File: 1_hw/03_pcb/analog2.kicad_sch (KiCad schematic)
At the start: 19 parts, among them U22 TPL0401B-10, U23 THS3491, U24 ADG1219BRJZ

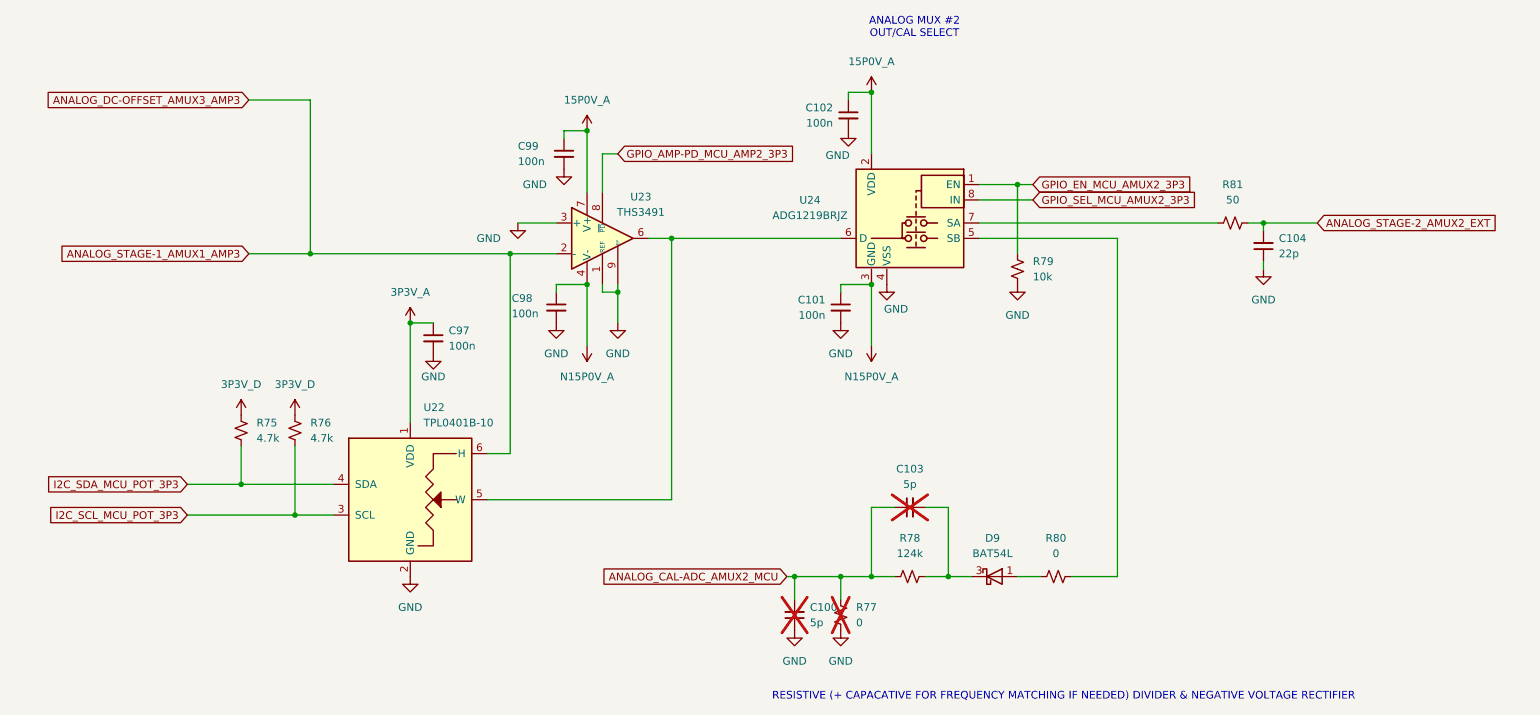
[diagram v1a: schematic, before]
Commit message: FEAT: Initial board placement started.
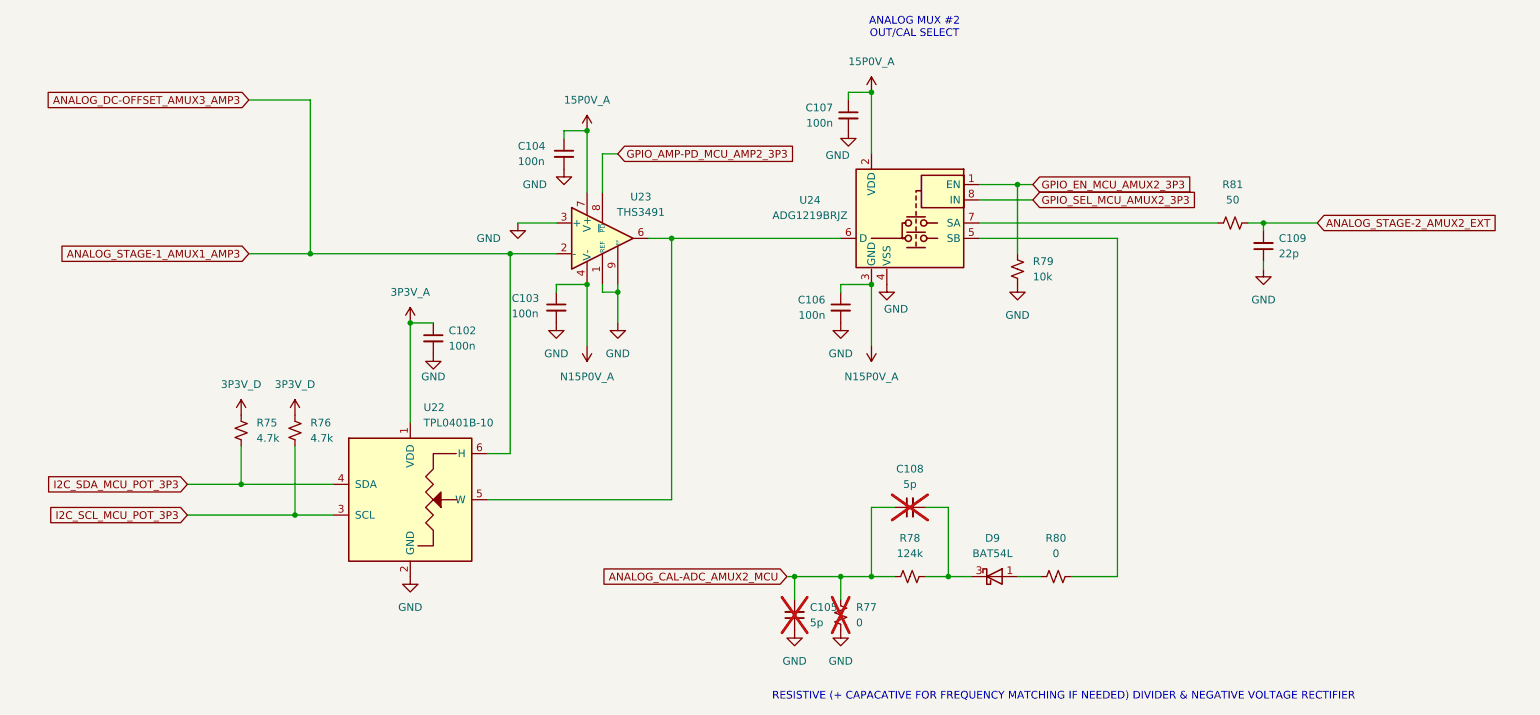
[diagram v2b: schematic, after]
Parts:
- renumbered C97 to C102, C98 to C103, C99 to C104, C100 to C105, C101 to C106, C102 to C107, C103 to C108, C104 to C109
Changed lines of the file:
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@@
 		(dnp no)
 		(fields_autoplaced yes)
-		(property "Reference" "#PWR0260"
+		(property "Reference" "#PWR0272"
 			(at 152.4 104.14 0)
 			(effects
@@
 			(project "arb"
 				(path "/866ef9be-3b01-4288-a6e0-a2357aa17e50/e46c6640-71a3-4b78-b602-0f6be9676e36"
-					(reference "#PWR0260")
+					(reference "#PWR0272")
 					(unit 1)
 				)
@@
 		(dnp no)
 		(fields_autoplaced yes)
-		(property "Reference" "#PWR0261"
+		(property "Reference" "#PWR0273"
 			(at 152.4 154.94 0)
 			(effects
@@
 			(project "arb"
 				(path "/866ef9be-3b01-4288-a6e0-a2357aa17e50/e46c6640-71a3-4b78-b602-0f6be9676e36"
-					(reference "#PWR0261")
+					(reference "#PWR0273")
 					(unit 1)
 				)
@@
 		(dnp no)
 		(fields_autoplaced yes)
-		(property "Reference" "#PWR0257"
+		(property "Reference" "#PWR0269"
 			(at 110.49 97.79 0)
 			(effects
@@
 			(project "arb"
 				(path "/866ef9be-3b01-4288-a6e0-a2357aa17e50/e46c6640-71a3-4b78-b602-0f6be9676e36"
-					(reference "#PWR0257")
+					(reference "#PWR0269")
 					(unit 1)
 				)
@@
 		(dnp no)
 		(fields_autoplaced yes)
-		(property "Reference" "C102"
+		(property "Reference" "C107"
 			(at 151.13 62.2363 0)
 			(effects
@@
 			(project "arb"
 				(path "/866ef9be-3b01-4288-a6e0-a2357aa17e50/e46c6640-71a3-4b78-b602-0f6be9676e36"
-					(reference "C102")
+					(reference "C107")
 					(unit 1)
 				)
@@
 		(dnp no)
 		(fields_autoplaced yes)
-		(property "Reference" "#PWR0259"
+		(property "Reference" "#PWR0271"
 			(at 144.78 154.94 0)
 			(effects
@@
 			(project "arb"
 				(path "/866ef9be-3b01-4288-a6e0-a2357aa17e50/e46c6640-71a3-4b78-b602-0f6be9676e36"
-					(reference "#PWR0259")
+					(reference "#PWR0271")
 					(unit 1)
 				)
@@
 		(on_board yes)
 		(dnp no)
-		(property "Reference" "#PWR0262"
+		(property "Reference" "#PWR0274"
 			(at 153.67 72.39 0)
 			(effects
@@
 			(project "arb"
 				(path "/866ef9be-3b01-4288-a6e0-a2357aa17e50/e46c6640-71a3-4b78-b602-0f6be9676e36"
-					(reference "#PWR0262")
+					(reference "#PWR0274")
 					(unit 1)
 				)
@@
 		(dnp yes)
 		(fields_autoplaced yes)
-		(property "Reference" "C100"
+		(property "Reference" "C105"
 			(at 147.32 144.7735 0)
 			(effects
@@
 			(project "arb"
 				(path "/866ef9be-3b01-4288-a6e0-a2357aa17e50/e46c6640-71a3-4b78-b602-0f6be9676e36"
-					(reference "C100")
+					(reference "C105")
 					(unit 1)
 				)
@@
 		(on_board yes)
 		(dnp no)
-		(property "Reference" "C99"
+		(property "Reference" "C104"
 			(at 99.06 68.58 0)
 			(effects
@@
 			(project "arb"
 				(path "/866ef9be-3b01-4288-a6e0-a2357aa17e50/e46c6640-71a3-4b78-b602-0f6be9676e36"
-					(reference "C99")
+					(reference "C104")
 					(unit 1)
 				)
@@
 		(dnp no)
 		(fields_autoplaced yes)
-		(property "Reference" "C101"
+		(property "Reference" "C106"
 			(at 149.86 93.9863 0)
 			(effects
@@
 			(project "arb"
 				(path "/866ef9be-3b01-4288-a6e0-a2357aa17e50/e46c6640-71a3-4b78-b602-0f6be9676e36"
-					(reference "C101")
+					(reference "C106")
 					(unit 1)
 				)
@@
 		(dnp no)
 		(fields_autoplaced yes)
-		(property "Reference" "#PWR0258"
+		(property "Reference" "#PWR0270"
 			(at 115.57 104.14 0)
 			(effects
@@
 			(project "arb"
 				(path "/866ef9be-3b01-4288-a6e0-a2357aa17e50/e46c6640-71a3-4b78-b602-0f6be9676e36"
-					(reference "#PWR0258")
+					(reference "#PWR0270")
 					(unit 1)
 				)
@@
 		(on_board yes)
 		(dnp no)
-		(property "Reference" "#PWR0255"
+		(property "Reference" "#PWR0267"
 			(at 106.68 78.74 0)
 			(effects
@@
 			(project "arb"
 				(path "/866ef9be-3b01-4288-a6e0-a2357aa17e50/e46c6640-71a3-4b78-b602-0f6be9676e36"
-					(reference "#PWR0255")
+					(reference "#PWR0267")
 					(unit 1)
 				)
@@
 		(on_board yes)
 		(dnp no)
-		(property "Reference" "C98"
+		(property "Reference" "C103"
 			(at 98.044 93.726 0)
 			(effects
@@
 			(project "arb"
 				(path "/866ef9be-3b01-4288-a6e0-a2357aa17e50/e46c6640-71a3-4b78-b602-0f6be9676e36"
-					(reference "C98")
+					(reference "C103")
 					(unit 1)
 				)
@@
 		(dnp no)
 		(fields_autoplaced yes)
-		(property "Reference" "#PWR0250"
+		(property "Reference" "#PWR0262"
 			(at 81.28 101.6 0)
 			(effects
@@
 			(project "arb"
 				(path "/866ef9be-3b01-4288-a6e0-a2357aa17e50/e46c6640-71a3-4b78-b602-0f6be9676e36"
-					(reference "#PWR0250")
+					(reference "#PWR0262")
 					(unit 1)
 				)
@@
 		(dnp no)
 		(fields_autoplaced yes)
-		(property "Reference" "#PWR0266"
+		(property "Reference" "#PWR0278"
 			(at 181.61 97.79 0)
 			(effects
@@
 			(project "arb"
 				(path "/866ef9be-3b01-4288-a6e0-a2357aa17e50/e46c6640-71a3-4b78-b602-0f6be9676e36"
-					(reference "#PWR0266")
+					(reference "#PWR0278")
 					(unit 1)
 				)
@@
 		(dnp no)
 		(fields_autoplaced yes)
-		(property "Reference" "#PWR0264"
+		(property "Reference" "#PWR0276"
 			(at 157.48 97.79 0)
 			(effects
@@
 			(project "arb"
 				(path "/866ef9be-3b01-4288-a6e0-a2357aa17e50/e46c6640-71a3-4b78-b602-0f6be9676e36"
-					(reference "#PWR0264")
+					(reference "#PWR0276")
 					(unit 1)
 				)
@@
 		(dnp no)
 		(fields_autoplaced yes)
-		(property "Reference" "#PWR0248"
+		(property "Reference" "#PWR0260"
 			(at 53.34 116.84 0)
 			(effects
@@
 			(project "arb"
 				(path "/866ef9be-3b01-4288-a6e0-a2357aa17e50/e46c6640-71a3-4b78-b602-0f6be9676e36"
-					(reference "#PWR0248")
+					(reference "#PWR0260")
 					(unit 1)
 				)
@@
 		(dnp yes)
 		(fields_autoplaced yes)
-		(property "Reference" "C103"
+		(property "Reference" "C108"
 			(at 163.8363 121.92 90)
 			(effects
@@
 			(project "arb"
 				(path "/866ef9be-3b01-4288-a6e0-a2357aa17e50/e46c6640-71a3-4b78-b602-0f6be9676e36"
-					(reference "C103")
+					(reference "C108")
 					(unit 1)
 				)
@@
 		(on_board yes)
 		(dnp no)
-		(property "Reference" "#PWR0265"
+		(property "Reference" "#PWR0277"
 			(at 160.02 97.79 0)
 			(effects
@@
 			(project "arb"
 				(path "/866ef9be-3b01-4288-a6e0-a2357aa17e50/e46c6640-71a3-4b78-b602-0f6be9676e36"
-					(reference "#PWR0265")
+					(reference "#PWR0277")
 					(unit 1)
 				)
@@
 		(dnp no)
 		(fields_autoplaced yes)
-		(property "Reference" "#PWR0254"
+		(property "Reference" "#PWR0266"
 			(at 105.41 104.14 0)
 			(effects
@@
 			(project "arb"
 				(path "/866ef9be-3b01-4288-a6e0-a2357aa17e50/e46c6640-71a3-4b78-b602-0f6be9676e36"
-					(reference "#PWR0254")
+					(reference "#PWR0266")
 					(unit 1)
 				)
@@
 		(dnp no)
 		(fields_autoplaced yes)
-		(property "Reference" "#PWR0249"
+		(property "Reference" "#PWR0261"
 			(at 62.23 116.84 0)
 			(effects
@@
 			(project "arb"
 				(path "/866ef9be-3b01-4288-a6e0-a2357aa17e50/e46c6640-71a3-4b78-b602-0f6be9676e36"
-					(reference "#PWR0249")
+					(reference "#PWR0261")
 					(unit 1)
 				)
@@
 		(dnp no)
 		(fields_autoplaced yes)
-		(property "Reference" "#PWR0251"
+		(property "Reference" "#PWR0263"
 			(at 81.28 146.05 0)
 			(effects
@@
 			(project "arb"
 				(path "/866ef9be-3b01-4288-a6e0-a2357aa17e50/e46c6640-71a3-4b78-b602-0f6be9676e36"
-					(reference "#PWR0251")
+					(reference "#PWR0263")
 					(unit 1)
 				)
@@
 		(dnp no)
 		(fields_autoplaced yes)
-		(property "Reference" "C97"
+		(property "Reference" "C102"
 			(at 87.63 99.0663 0)
 			(effects
@@
 			(project "arb"
 				(path "/866ef9be-3b01-4288-a6e0-a2357aa17e50/e46c6640-71a3-4b78-b602-0f6be9676e36"
-					(reference "C97")
+					(reference "C102")
 					(unit 1)
 				)
@@
 		(on_board yes)
 		(dnp no)
-		(property "Reference" "#PWR0252"
+		(property "Reference" "#PWR0264"
 			(at 85.09 109.22 0)
 			(effects
@@
 			(project "arb"
 				(path "/866ef9be-3b01-4288-a6e0-a2357aa17e50/e46c6640-71a3-4b78-b602-0f6be9676e36"
-					(reference "#PWR0252")
+					(reference "#PWR0264")
 					(unit 1)
 				)
@@
 		(dnp no)
 		(fields_autoplaced yes)
-		(property "Reference" "C104"
+		(property "Reference" "C109"
 			(at 224.79 83.8135 0)
 			(effects
@@
 			(project "arb"
 				(path "/866ef9be-3b01-4288-a6e0-a2357aa17e50/e46c6640-71a3-4b78-b602-0f6be9676e36"
-					(reference "C104")
+					(reference "C109")
 					(unit 1)
 				)
@@
 		(dnp no)
 		(fields_autoplaced yes)
-		(property "Reference" "#PWR0263"
+		(property "Reference" "#PWR0275"
 			(at 157.48 63.5 0)
 			(effects
@@
 			(project "arb"
 				(path "/866ef9be-3b01-4288-a6e0-a2357aa17e50/e46c6640-71a3-4b78-b602-0f6be9676e36"
-					(reference "#PWR0263")
+					(reference "#PWR0275")
 					(unit 1)
 				)
@@
 		(dnp no)
 		(fields_autoplaced yes)
-		(property "Reference" "#PWR0256"
+		(property "Reference" "#PWR0268"
 			(at 110.49 69.85 0)
 			(effects
@@
 			(project "arb"
 				(path "/866ef9be-3b01-4288-a6e0-a2357aa17e50/e46c6640-71a3-4b78-b602-0f6be9676e36"
-					(reference "#PWR0256")
+					(reference "#PWR0268")
 					(unit 1)
 				)
@@
 		(dnp no)
 		(fields_autoplaced yes)
-		(property "Reference" "#PWR0267"
+		(property "Reference" "#PWR0279"
 			(at 222.25 95.25 0)
 			(effects
@@
 			(project "arb"
 				(path "/866ef9be-3b01-4288-a6e0-a2357aa17e50/e46c6640-71a3-4b78-b602-0f6be9676e36"
-					(reference "#PWR0267")
+					(reference "#PWR0279")
 					(unit 1)
 				)
@@
 		(on_board yes)
 		(dnp no)
-		(property "Reference" "#PWR0253"
+		(property "Reference" "#PWR0265"
 			(at 99.06 87.63 0)
 			(effects
@@
 			(project "arb"
 				(path "/866ef9be-3b01-4288-a6e0-a2357aa17e50/e46c6640-71a3-4b78-b602-0f6be9676e36"
-					(reference "#PWR0253")
-					(unit 1)
-				)
+					(reference "#PWR0265")
+					(unit 1)
+				)
